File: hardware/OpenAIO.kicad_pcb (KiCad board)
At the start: 6 copper layers, 0 parts

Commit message: Net classes: patterns checked against the per-sheet netlists
VBAT, Phase, Power, Gate (driver outputs only), USB, RF, Analog; priorities
0..6, Default last. Wire widths 12 mil on VBAT and Phase, 8 on Power. Every
pattern verified to match at least one existing net; HIN/LIN, buses and
control signals stay Default.
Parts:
- added AE1: 47948-0001, OpenRX-Shared:ANT-SMD_47948-0001, F.Cu at (138.4, 108.8)
- added AE2: 2450AT18A100E, OpenRX-Shared:ANT-SMD_L3.2-W1.6, F.Cu at (133.5, 108.1)
- added C1: 100n, Capacitor_SMD:C_0201_0603Metric, F.Cu at (122.2, 72.0)
- added C10: 20p, Capacitor_SMD:C_0201_0603Metric, F.Cu at (124.7, 72.0)
- added C11: 100n, Capacitor_SMD:C_0201_0603Metric, F.Cu at (124.7, 73.7)
- added C12: 100n, Capacitor_SMD:C_0201_0603Metric, F.Cu at (124.7, 75.5)
- added C13: 100n, Capacitor_SMD:C_0201_0603Metric, F.Cu at (124.7, 77.2)
- added C14: 100n, Capacitor_SMD:C_0201_0603Metric, F.Cu at (124.7, 79.0)
- added C15: 4.7uF, Capacitor_SMD:C_0402_1005Metric, F.Cu at (141.7, 83.1)
- added C16: 4.7uF, Capacitor_SMD:C_0402_1005Metric, F.Cu at (141.7, 85.0)
- added C17: 4.7uF, Capacitor_SMD:C_0402_1005Metric, F.Cu at (141.7, 87.0)
- added C18: 4.7uF 50v, Capacitor_SMD:C_0805_2012Metric, F.Cu at (81.8, 13.2)
- added C19: 4.7uF 50v, Capacitor_SMD:C_0805_2012Metric, F.Cu at (81.8, 16.2)
- added C2: 100n, Capacitor_SMD:C_0201_0603Metric, F.Cu at (122.2, 73.7)
- added C20: 100n, Capacitor_SMD:C_0201_0603Metric, F.Cu at (64.7, 12.5)
- added C21: 100n, Capacitor_SMD:C_0201_0603Metric, F.Cu at (64.7, 14.3)
- added C22: 100nF, Capacitor_SMD:C_0201_0603Metric, F.Cu at (64.7, 16.0)
- added C23: 22uF, Capacitor_SMD:C_0603_1608Metric, F.Cu at (82.3, 24.6)
- added C24: 22uF, Capacitor_SMD:C_0603_1608Metric, F.Cu at (82.3, 27.1)
- added C25: 4.7uF, Capacitor_SMD:C_0402_1005Metric, F.Cu at (65.0, 28.4)
- added C26: 100n, Capacitor_SMD:C_0201_0603Metric, F.Cu at (64.7, 17.8)
- added C27: 22uF, Capacitor_SMD:C_0402_1005Metric, F.Cu at (65.0, 30.3)
- added C28: 22uF, Capacitor_SMD:C_0402_1005Metric, F.Cu at (65.0, 32.3)
- added C29: 100n, Capacitor_SMD:C_0201_0603Metric, F.Cu at (169.5, 72.0)
- added C3: 4.7uF, Capacitor_SMD:C_0402_1005Metric, F.Cu at (141.7, 81.1)
- added C30: 100n, Capacitor_SMD:C_0201_0603Metric, F.Cu at (169.5, 73.7)
- added C31: 470p, Capacitor_SMD:C_0201_0603Metric, F.Cu at (162.0, 95.6)
- added C32: 100n, Capacitor_SMD:C_0201_0603Metric, F.Cu at (162.0, 97.4)
- added C33: 1uF, Capacitor_SMD:C_0402_1005Metric, F.Cu at (169.6, 95.7)
- added C34: 100n, Capacitor_SMD:C_0201_0603Metric, F.Cu at (162.0, 99.1)
- added C35: 100n, Capacitor_SMD:C_0201_0603Metric, F.Cu at (162.0, 100.9)
- added C36: 100n, Capacitor_SMD:C_0201_0603Metric, F.Cu at (146.7, 103.1)
- added C37: 100nF, Capacitor_SMD:C_0201_0603Metric, F.Cu at (139.7, 7.56)
- added C38: 100nF, Capacitor_SMD:C_0201_0603Metric, F.Cu at (139.7, 9.31)
- added C39: 100nF, Capacitor_SMD:C_0201_0603Metric, F.Cu at (139.7, 11.1)
- added C4: 20p, Capacitor_SMD:C_0201_0603Metric, F.Cu at (122.2, 75.5)
- added C40: 100nF, Capacitor_SMD:C_0402_WIDE, F.Cu at (142.9, 18.2)
- added C41: 100nF, Capacitor_SMD:C_0402_WIDE, F.Cu at (142.9, 20.1)
- added C42: 100nF, Capacitor_SMD:C_0402_WIDE, F.Cu at (142.9, 22.1)
- added C43: 100nF, Capacitor_SMD:C_0201_0603Metric, F.Cu at (139.7, 12.8)
- added C44: 100nF, Capacitor_SMD:C_0201_0603Metric, F.Cu at (105.4, 8.14)
- added C45: 100nF, Capacitor_SMD:C_0201_0603Metric, F.Cu at (105.4, 9.89)
- added C46: 100nF, Capacitor_SMD:C_0201_0603Metric, F.Cu at (105.4, 11.6)
- added C47: 100nF, Capacitor_SMD:C_0402_WIDE, F.Cu at (108.6, 18.8)
- added C48: 100nF, Capacitor_SMD:C_0402_WIDE, F.Cu at (108.6, 20.7)
- added C49: 100nF, Capacitor_SMD:C_0402_WIDE, F.Cu at (108.6, 22.7)
- added C5: 100n, Capacitor_SMD:C_0201_0603Metric, F.Cu at (122.2, 77.2)
- added C50: 100nF, Capacitor_SMD:C_0201_0603Metric, F.Cu at (105.4, 13.4)
- added C51: 100nF, Capacitor_SMD:C_0201_0603Metric, F.Cu at (122.3, 8.31)
- added C52: 100nF, Capacitor_SMD:C_0201_0603Metric, F.Cu at (122.3, 10.1)
- added C53: 100nF, Capacitor_SMD:C_0201_0603Metric, F.Cu at (122.3, 11.8)
- added C54: 100nF, Capacitor_SMD:C_0402_WIDE, F.Cu at (125.6, 18.9)
- added C55: 100nF, Capacitor_SMD:C_0402_WIDE, F.Cu at (125.6, 20.9)
- added C56: 100nF, Capacitor_SMD:C_0402_WIDE, F.Cu at (125.6, 22.9)
- added C57: 100nF, Capacitor_SMD:C_0201_0603Metric, F.Cu at (122.3, 13.6)
- added C58: 100nF, Capacitor_SMD:C_0201_0603Metric, F.Cu at (157.1, 7.17)
- added C59: 100nF, Capacitor_SMD:C_0201_0603Metric, F.Cu at (157.1, 8.92)
- added C6: 100n, Capacitor_SMD:C_0201_0603Metric, F.Cu at (122.2, 79.0)
- added C60: 100nF, Capacitor_SMD:C_0201_0603Metric, F.Cu at (157.1, 10.7)
- added C61: 100nF, Capacitor_SMD:C_0402_WIDE, F.Cu at (160.4, 17.8)
- added C62: 100nF, Capacitor_SMD:C_0402_WIDE, F.Cu at (160.4, 19.8)
- added C63: 100nF, Capacitor_SMD:C_0402_WIDE, F.Cu at (160.4, 21.7)
- added C64: 100nF, Capacitor_SMD:C_0201_0603Metric, F.Cu at (157.1, 12.4)
- added C65: 100nF, Capacitor_SMD:C_0201_0603Metric, F.Cu at (122.2, 94.4)
- added C66: 100nF, Capacitor_SMD:C_0201_0603Metric, F.Cu at (122.2, 96.2)
- added C67: 10nF, Capacitor_SMD:C_0201_0603Metric, F.Cu at (122.2, 97.9)
- added C68: 470nF, Capacitor_SMD:C_0201_0603Metric, F.Cu at (122.2, 99.7)
- added C69: 1nF, Capacitor_SMD:C_0201_0603Metric, F.Cu at (122.2, 101.4)
- added C7: 100n, Capacitor_SMD:C_0201_0603Metric, F.Cu at (122.2, 80.7)
- added C70: 100nF, Capacitor_SMD:C_0201_0603Metric, F.Cu at (122.2, 103.2)
- added C71: 100nF, Capacitor_SMD:C_0201_0603Metric, F.Cu at (122.2, 104.9)
- added C72: 15pF, Capacitor_SMD:C_0201_0603Metric, F.Cu at (122.2, 106.7)
- added C73: 10nF, Capacitor_SMD:C_0201_0603Metric, F.Cu at (124.7, 94.4)
- added C74: 15pF, Capacitor_SMD:C_0201_0603Metric, F.Cu at (124.7, 96.2)
- added C75: 10uF, Capacitor_SMD:C_0402_1005Metric, F.Cu at (139.9, 94.5)
- added C76: 100nF, Capacitor_SMD:C_0201_0603Metric, F.Cu at (124.7, 97.9)
- added C77: 1uF, Capacitor_SMD:C_0201_0603Metric, F.Cu at (124.7, 99.7)
- added C78: 100nF, Capacitor_SMD:C_0201_0603Metric, F.Cu at (124.7, 101.4)
- added C79: 100nF, Capacitor_SMD:C_0201_0603Metric, F.Cu at (124.7, 103.2)
- added C8: 100n, Capacitor_SMD:C_0201_0603Metric, F.Cu at (122.2, 82.5)
- added C80: 10nF, Capacitor_SMD:C_0201_0603Metric, F.Cu at (124.7, 104.9)
- added C81: 1uF, Capacitor_SMD:C_0201_0603Metric, F.Cu at (124.7, 106.7)
- added C82: 10uF, Capacitor_SMD:C_0402_1005Metric, F.Cu at (139.9, 96.5)
- added C83: 1uF, Capacitor_SMD:C_0201_0603Metric, F.Cu at (127.1, 94.4)
- added C84: 1uF, Capacitor_SMD:C_0201_0603Metric, F.Cu at (127.1, 96.2)
- added C85: 1uF, Capacitor_SMD:C_0201_0603Metric, F.Cu at (127.1, 97.9)
- added C86: 1uF, Capacitor_SMD:C_0201_0603Metric, F.Cu at (127.1, 99.7)
- added C87: 1.2pF, Capacitor_SMD:C_0201_0603Metric, F.Cu at (127.1, 101.4)
- added C88: 10uF, Capacitor_SMD:C_0402_1005Metric, F.Cu at (139.9, 98.5)
- added C89: 1.2pF, Capacitor_SMD:C_0201_0603Metric, F.Cu at (127.1, 103.2)
- added C9: 100n, Capacitor_SMD:C_0201_0603Metric, F.Cu at (122.2, 84.2)
- added Card1: TF-021B-H265, lib:TF-SMD_TF-021B-H265, F.Cu at (152.2, 98.4)
- added D1: LED_1_Blue, LED_SMD:LED_0402_1005Metric, F.Cu at (122.7, 89.3)
- added D2: DSK24, lib:SOD-123_L2.8-W1.8-LS3.7-RD, F.Cu at (70.8, 24.7)
- added D3: DSK24, lib:SOD-123_L2.8-W1.8-LS3.7-RD, F.Cu at (70.8, 27.6)
- added D4: LED_1_Green, LED_SMD:LED_0402_1005Metric, F.Cu at (75.1, 24.3)
- added D5: LED_1_Green, LED_SMD:LED_0402_1005Metric, F.Cu at (75.1, 26.3)
- added D6: LED_1_Green, LED_SMD:LED_0402_1005Metric, F.Cu at (75.1, 28.3)
- added D7: LED_1_Green, LED_SMD:LED_0402_1005Metric, F.Cu at (75.1, 30.3)
- added D8: SDM02U30LP3-7B, lib:X3-DFN0603-2_L0.6-W0.3-RD, F.Cu at (169.3, 99.8)
- added D9: XL-1010RGBC-WS2812B, OpenRX-Shared:LED-SMD_4P-L1.0-W1.0-TL_XL-1010RGBC-WS2812B, F.Cu at (128.9, 108.9)
- added FL1: 2450FM07D0034T, OpenRX-Shared:FILTER-SMD_4P-L1.0-W0.5-L, F.Cu at (126.1, 111.3)
- added J1: 5V, lib:small_pad, F.Cu at (105.7, 102.4)
- added J10: 5V, lib:small_pad, F.Cu at (112.3, 104.8)
- added J11: 5V, lib:small_pad, F.Cu at (112.3, 107.2)
- added J12: 5V, lib:small_pad, F.Cu at (112.3, 109.6)
- added J13: 5V, lib:small_pad, F.Cu at (67.1, 47.0)
- added J14: 5V, lib:small_pad, F.Cu at (69.5, 47.0)
- added J2: 5V, lib:small_pad, F.Cu at (105.7, 104.8)
- added J21: 5V, lib:small_pad, F.Cu at (124.7, 46.0)
- added J23: 5V, lib:small_pad, F.Cu at (124.7, 48.4)
- added J25: 5V, lib:small_pad, F.Cu at (124.7, 50.8)
- added J26: 5V, lib:small_pad, F.Cu at (124.7, 53.2)
- added J28: 5V, lib:small_pad, F.Cu at (124.7, 55.6)
- added J29: 5V, lib:small_pad, F.Cu at (124.7, 58.0)
- added J3: 5V, lib:small_pad, F.Cu at (105.7, 107.2)
- added J30: 5V, lib:small_pad, F.Cu at (128.0, 46.0)
- added J32: 5V, lib:small_pad, F.Cu at (128.0, 48.4)
- added J33: 5V, lib:small_pad, F.Cu at (128.0, 50.8)
- added J34: 5V, lib:small_pad, F.Cu at (128.0, 53.2)
- added J35: 5V, lib:small_pad, F.Cu at (128.0, 55.6)
- added J36: 5V, lib:small_pad, F.Cu at (128.0, 58.0)
- added J37: 5V, lib:small_pad, F.Cu at (131.3, 46.0)
- added J38: 5V, lib:small_pad, F.Cu at (131.3, 48.4)
- added J39: 5V, lib:small_pad, F.Cu at (131.3, 50.8)
- added J4: 5V, lib:small_pad, F.Cu at (105.7, 109.6)
- added J42: 5V, lib:small_pad, F.Cu at (131.3, 53.2)
- added J43: 5V, lib:small_pad, F.Cu at (131.3, 55.6)
- added J44: 5V, lib:small_pad, F.Cu at (131.3, 58.0)
- added J45: 5V, lib:small_pad, F.Cu at (134.6, 46.0)
- added J48: 5V, lib:small_pad, F.Cu at (134.6, 48.4)
- added J49: 5V, lib:small_pad, F.Cu at (134.6, 50.8)
- added J5: 5V, lib:small_pad, F.Cu at (109.0, 102.4)
- added J50: 5V, lib:small_pad, F.Cu at (134.6, 53.2)
- added J51: 5V, lib:small_pad, F.Cu at (134.6, 55.6)
- added J6: 5V, lib:small_pad, F.Cu at (109.0, 104.8)
- added J7: 5V, lib:small_pad, F.Cu at (109.0, 107.2)
- added J8: 5V, lib:small_pad, F.Cu at (109.0, 109.6)
- added J9: 5V, lib:small_pad, F.Cu at (112.3, 102.4)
- added L1: AOTA-B201610S3R3-101-T, lib:IND-SMD_L2.0-W1.6_AOTA-B201610S3R3-101-T, F.Cu at (127.7, 86.9)
- added L2: XRTC303020D4R7MBCA, lib:IND-SMD_L3.0-W3.0_AFE303020S, F.Cu at (70.2, 21.0)
- added L3: XRTC303020D4R7MBCA, lib:IND-SMD_L3.0-W3.0_AFE303020S, F.Cu at (74.5, 21.0)
- added L4: 15uH, Inductor_SMD:L_0805_2012Metric, F.Cu at (133.1, 111.0)
- added L5: 24nH, Inductor_SMD:L_0201_0603Metric, F.Cu at (127.1, 104.9)
- added L6: 2.0nH, Inductor_SMD:L_0201_0603Metric, F.Cu at (127.1, 106.7)
- added L7: 2.5nH, Inductor_SMD:L_0201_0603Metric, F.Cu at (129.6, 94.4)
- added OSC1: OW7EL89CENUNFAYLC-52M, OpenRX-Shared:OSC-SMD_4P-L2.0-W1.6-BL_TXC_7Z, F.Cu at (138.8, 102.3)
- added Q1: AP1606, lib:DFN-3L_L1.0-W0.6-P0.65-BR, F.Cu at (141.4, 88.9)
- added Q10: DOY180N03T, Package_SON:Diodes_PowerDI3333-8, F.Cu at (101.8, 14.4)
- added Q11: DOY180N03T, Package_SON:Diodes_PowerDI3333-8, F.Cu at (101.8, 19.1)
- added Q12: DOY180N03T, Package_SON:Diodes_PowerDI3333-8, F.Cu at (101.8, 23.8)
- added Q13: DOY180N03T, Package_SON:Diodes_PowerDI3333-8, F.Cu at (101.8, 28.5)
- added Q14: DOY180N03T, Package_SON:Diodes_PowerDI3333-8, F.Cu at (101.8, 33.2)
- added Q15: DOY180N03T, Package_SON:Diodes_PowerDI3333-8, F.Cu at (118.7, 9.93)
- added Q16: DOY180N03T, Package_SON:Diodes_PowerDI3333-8, F.Cu at (118.7, 14.6)
- added Q17: DOY180N03T, Package_SON:Diodes_PowerDI3333-8, F.Cu at (118.7, 19.3)
- added Q18: DOY180N03T, Package_SON:Diodes_PowerDI3333-8, F.Cu at (118.7, 24.0)
- added Q19: DOY180N03T, Package_SON:Diodes_PowerDI3333-8, F.Cu at (118.7, 28.7)
- added Q2: AP1606, lib:DFN-3L_L1.0-W0.6-P0.65-BR, F.Cu at (141.4, 90.7)
- added Q20: DOY180N03T, Package_SON:Diodes_PowerDI3333-8, F.Cu at (118.7, 33.4)
- added Q21: DOY180N03T, Package_SON:Diodes_PowerDI3333-8, F.Cu at (153.5, 8.79)
- added Q22: DOY180N03T, Package_SON:Diodes_PowerDI3333-8, F.Cu at (153.5, 13.5)
- added Q23: DOY180N03T, Package_SON:Diodes_PowerDI3333-8, F.Cu at (153.5, 18.2)
- added Q24: DOY180N03T, Package_SON:Diodes_PowerDI3333-8, F.Cu at (153.5, 22.9)
- added Q25: DOY180N03T, Package_SON:Diodes_PowerDI3333-8, F.Cu at (153.5, 27.5)
- added Q26: DOY180N03T, Package_SON:Diodes_PowerDI3333-8, F.Cu at (153.5, 32.2)
- added Q3: DOY180N03T, Package_SON:Diodes_PowerDI3333-8, F.Cu at (136.1, 9.18)
- added Q4: DOY180N03T, Package_SON:Diodes_PowerDI3333-8, F.Cu at (136.1, 13.9)
- added Q5: DOY180N03T, Package_SON:Diodes_PowerDI3333-8, F.Cu at (136.1, 18.6)
- added Q6: DOY180N03T, Package_SON:Diodes_PowerDI3333-8, F.Cu at (136.1, 23.2)
- added Q7: DOY180N03T, Package_SON:Diodes_PowerDI3333-8, F.Cu at (136.1, 27.9)
- added Q8: DOY180N03T, Package_SON:Diodes_PowerDI3333-8, F.Cu at (136.1, 32.6)
- added Q9: DOY180N03T, Package_SON:Diodes_PowerDI3333-8, F.Cu at (101.8, 9.76)
- added R1: 100k, Resistor_SMD:R_0201_0603Metric, F.Cu at (124.7, 80.7)
- added R10: 30R, Resistor_SMD:R_0201_0603Metric, F.Cu at (127.1, 82.5)
- added R100: 15R, Resistor_SMD:R_0201_0603Metric, F.Cu at (162.0, 7.17)
- added R101: 15R, Resistor_SMD:R_0201_0603Metric, F.Cu at (162.0, 8.92)
- added R102: 10k, Resistor_SMD:R_0201_0603Metric, F.Cu at (162.0, 10.7)
- added R103: 1k, Resistor_SMD:R_0201_0603Metric, F.Cu at (162.0, 12.4)
- added R104: 10k, Resistor_SMD:R_0201_0603Metric, F.Cu at (162.0, 14.2)
- added R105: 10k, Resistor_SMD:R_0201_0603Metric, F.Cu at (162.0, 15.9)
- added R106: 1k, Resistor_SMD:R_0201_0603Metric, F.Cu at (164.5, 7.17)
- added R107: 10k, Resistor_SMD:R_0201_0603Metric, F.Cu at (164.5, 8.92)
- added R108: 10k, Resistor_SMD:R_0201_0603Metric, F.Cu at (164.5, 10.7)
- added R109: 1k, Resistor_SMD:R_0201_0603Metric, F.Cu at (164.5, 12.4)
- added R11: 5.1k, Resistor_SMD:R_0201_0603Metric, F.Cu at (127.1, 84.2)
- added R110: 10k, Resistor_SMD:R_0201_0603Metric, F.Cu at (164.5, 14.2)
- added R111: 10k, Resistor_SMD:R_0201_0603Metric, F.Cu at (129.6, 96.2)
- added R112: 10k, Resistor_SMD:R_0201_0603Metric, F.Cu at (129.6, 97.9)
- added R113: 10k, Resistor_SMD:R_0201_0603Metric, F.Cu at (129.6, 99.7)
- added R114: 10k, Resistor_SMD:R_0201_0603Metric, F.Cu at (129.6, 101.4)
- added R12: 5.1k, Resistor_SMD:R_0201_0603Metric, F.Cu at (129.6, 72.0)
- added R13: 100k, Resistor_SMD:R_0201_0603Metric, F.Cu at (129.6, 73.7)
- added R14: 2.4k, Resistor_SMD:R_0201_0603Metric, F.Cu at (129.6, 75.5)
- added R15: 75R, Resistor_SMD:R_0201_0603Metric, F.Cu at (129.6, 77.2)
- added R16: 75R, Resistor_SMD:R_0201_0603Metric, F.Cu at (129.6, 79.0)
- added R17: 100k, Resistor_SMD:R_0201_0603Metric, F.Cu at (67.2, 12.5)
- added R18: 6.49k, Resistor_SMD:R_0201_0603Metric, F.Cu at (67.2, 14.3)
- added R19: 100k, Resistor_SMD:R_0201_0603Metric, F.Cu at (67.2, 16.0)
- added R2: 10k, Resistor_SMD:R_0201_0603Metric, F.Cu at (124.7, 82.5)
- added R20: 13.7k, Resistor_SMD:R_0201_0603Metric, F.Cu at (67.2, 17.8)
- added R21: 7.5k, Resistor_SMD:R_0201_0603Metric, F.Cu at (69.6, 12.5)
- added R22: 2.4k, Resistor_SMD:R_0201_0603Metric, F.Cu at (69.6, 14.3)
- added R23: 6.49k, Resistor_SMD:R_0201_0603Metric, F.Cu at (69.6, 16.0)
- added R24: 510R, Resistor_SMD:R_0201_0603Metric, F.Cu at (69.6, 17.8)
- added R25: 10k, Resistor_SMD:R_0201_0603Metric, F.Cu at (169.5, 75.5)
- added R26: 75R, Resistor_SMD:R_0201_0603Metric, F.Cu at (164.5, 95.6)
- added R27: 3.9k, Resistor_SMD:R_0201_0603Metric, F.Cu at (164.5, 97.4)
- added R28: 12k, Resistor_SMD:R_0201_0603Metric, F.Cu at (164.5, 99.1)
- added R29: 1.4k, Resistor_SMD:R_0201_0603Metric, F.Cu at (164.5, 100.9)
- added R3: 5.1k, Resistor_SMD:R_0201_0603Metric, F.Cu at (124.7, 84.2)
- added R30: 680R, Resistor_SMD:R_0201_0603Metric, F.Cu at (166.9, 95.6)
- added R31: 510R, Resistor_SMD:R_0201_0603Metric, F.Cu at (166.9, 97.4)
- added R32: 510R, Resistor_SMD:R_0201_0603Metric, F.Cu at (166.9, 99.1)
- added R33: 75R, Resistor_SMD:R_0201_0603Metric, F.Cu at (166.9, 100.9)
- added R34: 10k, Resistor_SMD:R_0201_0603Metric, F.Cu at (146.7, 104.8)
- added R35: 15R, Resistor_SMD:R_0201_0603Metric, F.Cu at (139.7, 14.6)
- added R36: 15R, Resistor_SMD:R_0201_0603Metric, F.Cu at (139.7, 16.3)
- added R37: 10k, Resistor_SMD:R_0201_0603Metric, F.Cu at (142.1, 7.56)
- added R38: 10k, Resistor_SMD:R_0201_0603Metric, F.Cu at (142.1, 9.31)
- added R39: 220R, Resistor_SMD:R_0201_0603Metric, F.Cu at (142.1, 11.1)
- added R4: 5.1k, Resistor_SMD:R_0201_0603Metric, F.Cu at (127.1, 72.0)
- added R40: 10R, Resistor_SMD:R_0201_0603Metric, F.Cu at (142.1, 12.8)
- added R41: 15R, Resistor_SMD:R_0201_0603Metric, F.Cu at (142.1, 14.6)
- added R42: 15R, Resistor_SMD:R_0201_0603Metric, F.Cu at (142.1, 16.3)
- added R43: 15R, Resistor_SMD:R_0201_0603Metric, F.Cu at (144.6, 7.56)
- added R44: 15R, Resistor_SMD:R_0201_0603Metric, F.Cu at (144.6, 9.31)
- added R45: 10k, Resistor_SMD:R_0201_0603Metric, F.Cu at (144.6, 11.1)
- added R46: 1k, Resistor_SMD:R_0201_0603Metric, F.Cu at (144.6, 12.8)
- added R47: 10k, Resistor_SMD:R_0201_0603Metric, F.Cu at (144.6, 14.6)
- added R48: 10k, Resistor_SMD:R_0201_0603Metric, F.Cu at (144.6, 16.3)
- added R49: 1k, Resistor_SMD:R_0201_0603Metric, F.Cu at (147.0, 7.56)
- added R5: 1k, Resistor_SMD:R_0201_0603Metric, F.Cu at (127.1, 73.7)
- added R50: 10k, Resistor_SMD:R_0201_0603Metric, F.Cu at (147.0, 9.31)
- added R51: 10k, Resistor_SMD:R_0201_0603Metric, F.Cu at (147.0, 11.1)
- added R52: 1k, Resistor_SMD:R_0201_0603Metric, F.Cu at (147.0, 12.8)
- added R53: 10k, Resistor_SMD:R_0201_0603Metric, F.Cu at (147.0, 14.6)
- added R54: 15R, Resistor_SMD:R_0201_0603Metric, F.Cu at (105.4, 15.1)
- added R55: 15R, Resistor_SMD:R_0201_0603Metric, F.Cu at (105.4, 16.9)
- added R56: 10k, Resistor_SMD:R_0201_0603Metric, F.Cu at (107.8, 8.14)
- added R57: 10k, Resistor_SMD:R_0201_0603Metric, F.Cu at (107.8, 9.89)
- added R58: 220R, Resistor_SMD:R_0201_0603Metric, F.Cu at (107.8, 11.6)
- added R59: 10R, Resistor_SMD:R_0201_0603Metric, F.Cu at (107.8, 13.4)
- added R6: 1k, Resistor_SMD:R_0201_0603Metric, F.Cu at (127.1, 75.5)
- added R60: 15R, Resistor_SMD:R_0201_0603Metric, F.Cu at (107.8, 15.1)
- added R61: 15R, Resistor_SMD:R_0201_0603Metric, F.Cu at (107.8, 16.9)
- added R62: 15R, Resistor_SMD:R_0201_0603Metric, F.Cu at (110.3, 8.14)
- added R63: 15R, Resistor_SMD:R_0201_0603Metric, F.Cu at (110.3, 9.89)
- added R64: 10k, Resistor_SMD:R_0201_0603Metric, F.Cu at (110.3, 11.6)
- added R65: 1k, Resistor_SMD:R_0201_0603Metric, F.Cu at (110.3, 13.4)
- added R66: 10k, Resistor_SMD:R_0201_0603Metric, F.Cu at (110.3, 15.1)
- added R67: 10k, Resistor_SMD:R_0201_0603Metric, F.Cu at (110.3, 16.9)
- added R68: 1k, Resistor_SMD:R_0201_0603Metric, F.Cu at (112.7, 8.14)
- added R69: 10k, Resistor_SMD:R_0201_0603Metric, F.Cu at (112.7, 9.89)
- added R7: 10k, Resistor_SMD:R_0201_0603Metric, F.Cu at (127.1, 77.2)
- added R70: 10k, Resistor_SMD:R_0201_0603Metric, F.Cu at (112.7, 11.6)
- added R71: 1k, Resistor_SMD:R_0201_0603Metric, F.Cu at (112.7, 13.4)
- added R72: 10k, Resistor_SMD:R_0201_0603Metric, F.Cu at (112.7, 15.1)
- added R73: 15R, Resistor_SMD:R_0201_0603Metric, F.Cu at (122.3, 15.3)
- added R74: 15R, Resistor_SMD:R_0201_0603Metric, F.Cu at (122.3, 17.1)
- added R75: 10k, Resistor_SMD:R_0201_0603Metric, F.Cu at (124.7, 8.31)
- added R76: 10k, Resistor_SMD:R_0201_0603Metric, F.Cu at (124.7, 10.1)
- added R77: 220R, Resistor_SMD:R_0201_0603Metric, F.Cu at (124.7, 11.8)
- added R78: 10R, Resistor_SMD:R_0201_0603Metric, F.Cu at (124.7, 13.6)
- added R79: 15R, Resistor_SMD:R_0201_0603Metric, F.Cu at (124.7, 15.3)
- added R8: 30R, Resistor_SMD:R_0201_0603Metric, F.Cu at (127.1, 79.0)
- added R80: 15R, Resistor_SMD:R_0201_0603Metric, F.Cu at (124.7, 17.1)
- added R81: 15R, Resistor_SMD:R_0201_0603Metric, F.Cu at (127.2, 8.31)
- added R82: 15R, Resistor_SMD:R_0201_0603Metric, F.Cu at (127.2, 10.1)
- added R83: 10k, Resistor_SMD:R_0201_0603Metric, F.Cu at (127.2, 11.8)
- added R84: 1k, Resistor_SMD:R_0201_0603Metric, F.Cu at (127.2, 13.6)
- added R85: 10k, Resistor_SMD:R_0201_0603Metric, F.Cu at (127.2, 15.3)
- added R86: 10k, Resistor_SMD:R_0201_0603Metric, F.Cu at (127.2, 17.1)
- added R87: 1k, Resistor_SMD:R_0201_0603Metric, F.Cu at (129.6, 8.31)
- added R88: 10k, Resistor_SMD:R_0201_0603Metric, F.Cu at (129.6, 10.1)
- added R89: 10k, Resistor_SMD:R_0201_0603Metric, F.Cu at (129.6, 11.8)
- added R9: 30R, Resistor_SMD:R_0201_0603Metric, F.Cu at (127.1, 80.7)
- added R90: 1k, Resistor_SMD:R_0201_0603Metric, F.Cu at (129.6, 13.6)
- added R91: 10k, Resistor_SMD:R_0201_0603Metric, F.Cu at (129.6, 15.3)
- added R92: 15R, Resistor_SMD:R_0201_0603Metric, F.Cu at (157.1, 14.2)
- added R93: 15R, Resistor_SMD:R_0201_0603Metric, F.Cu at (157.1, 15.9)
- added R94: 10k, Resistor_SMD:R_0201_0603Metric, F.Cu at (159.6, 7.17)
- added R95: 10k, Resistor_SMD:R_0201_0603Metric, F.Cu at (159.6, 8.92)
- added R96: 220R, Resistor_SMD:R_0201_0603Metric, F.Cu at (159.6, 10.7)
- added R97: 10R, Resistor_SMD:R_0201_0603Metric, F.Cu at (159.6, 12.4)
- added R98: 15R, Resistor_SMD:R_0201_0603Metric, F.Cu at (159.6, 14.2)
- added R99: 15R, Resistor_SMD:R_0201_0603Metric, F.Cu at (159.6, 15.9)
- added Rsense1: 0.2mR, Resistor_SMD:R_2512_6332Metric, F.Cu at (69.5, 52.9)
- added TP1: TestPoint, TestPoint:TestPoint_Pad_D1.0mm, F.Cu at (140.0, 18.7)
- added TP2: TestPoint, TestPoint:TestPoint_Pad_D1.0mm, F.Cu at (140.0, 21.8)
- added TP3: TestPoint, TestPoint:TestPoint_Pad_D1.0mm, F.Cu at (105.7, 19.3)
- added TP4: TestPoint, TestPoint:TestPoint_Pad_D1.0mm, F.Cu at (105.7, 22.3)
- added TP5: TestPoint, TestPoint:TestPoint_Pad_D1.0mm, F.Cu at (122.6, 19.5)
- added TP6: TestPoint, TestPoint:TestPoint_Pad_D1.0mm, F.Cu at (122.6, 22.5)
- added TP7: TestPoint, TestPoint:TestPoint_Pad_D1.0mm, F.Cu at (157.4, 18.3)
- added TP8: TestPoint, TestPoint:TestPoint_Pad_D1.0mm, F.Cu at (157.4, 21.4)
- added TP9: BOOT, OpenRX-Shared:SolderPad_1.2x2.0mm, F.Cu at (122.6, 109.4)
- added U1: TS2306A 240GF MSM 9_C2976675, lib:SW-SMD_4P-L3.0-W2.0-P0.85-LS3.5, F.Cu at (123.4, 86.7)
- added U10: COS8051SOT, lib:SOT-23-5_L3.0-W1.7-P0.95-LS2.8-BR, F.Cu at (168.3, 103.8)
- added U11: TLV7031DPWR, lib:X2SON-4_L0.8-W0.8-P0.48-TL-A, F.Cu at (169.5, 97.8)
- added U12: SM06B-SRSS-TB(LF)(SN), lib:CONN-SMD_SM06B-SRSS-TB-LF-SN, F.Cu at (81.0, 74.6)
- added U13: AT32F421G8U7, 4in1ESC:QFN-28_L4.0-W4.0-P0.40-TL-EP2.4, F.Cu at (141.1, 31.3)
- added U14: NSG2065Q, 4in1ESC:QFN-24_L4.0-W4.0-P0.50-TL-EP2.8, F.Cu at (141.5, 26.0)
- added U15: AT32F421G8U7, 4in1ESC:QFN-28_L4.0-W4.0-P0.40-TL-EP2.4, F.Cu at (106.8, 31.9)
- added U16: NSG2065Q, 4in1ESC:QFN-24_L4.0-W4.0-P0.50-TL-EP2.8, F.Cu at (107.2, 26.6)
- added U17: AT32F421G8U7, 4in1ESC:QFN-28_L4.0-W4.0-P0.40-TL-EP2.4, F.Cu at (123.7, 32.1)
- added U18: NSG2065Q, 4in1ESC:QFN-24_L4.0-W4.0-P0.50-TL-EP2.8, F.Cu at (124.2, 26.8)
- added U19: AT32F421G8U7, 4in1ESC:QFN-28_L4.0-W4.0-P0.40-TL-EP2.4, F.Cu at (158.5, 30.9)
- added U2: RP2354A, lib:QFN-60_L7.0-W7.0-P0.40-TL-EP3.4, F.Cu at (135.8, 84.6)
- added U20: NSG2065Q, 4in1ESC:QFN-24_L4.0-W4.0-P0.50-TL-EP2.8, F.Cu at (159.0, 25.6)
- added U21: SX1281IMLTRT, OpenRX-Shared:QFN-24_L4.0-W4.0-P0.50-TL-EP2.6, F.Cu at (133.7, 103.7)
- added U22: ESP32-C3, Package_DFN_QFN:QFN-32-1EP_5x5mm_P0.5mm_EP3.7x3.7mm, F.Cu at (134.8, 97.2)
- added U23: TLV75533PDQNR, OpenRX-Shared:X2SON-4_L1.0-W1.0-P0.65-TL-EP, F.Cu at (128.8, 111.4)
- added U3: LMR51430YFDDCR, lib:SOT-23-6_L2.9-W1.6-P0.95-LS2.9-BL, F.Cu at (66.0, 20.8)
- added U4: LMR51430YFDDCR, lib:SOT-23-6_L2.9-W1.6-P0.95-LS2.9-BL, F.Cu at (66.0, 25.2)
- added U5: INA186A3IDCKR, 4in1ESC:SOT-363_SC-70-6, F.Cu at (70.2, 31.1)
- added U6: LP5912-1.8DRVR, lib:WSON-6-1EP_2x2mm_P0.65mm_EP1x1.6mm_ThermalVias, F.Cu at (78.4, 25.2)
- added U7: LP5912-3.3DRVR, Package_SON:WSON-6-1EP_2x2mm_P0.65mm_EP1x1.6mm, F.Cu at (78.4, 28.8)
- added U8: BMI270, lib:LGA-14_L3.0-W2.5-P0.50-BR, F.Cu at (172.9, 73.0)
- added U9: SN74LVC1G3157DTBR, lib:X2SON-6_L1.0-W0.8-BL, F.Cu at (163.4, 104.3)
- added USB1: TYPE-C 16P QTWT, lib:USB-TYPE-C-SMD_TYPE-C-16P-QTWT, F.Cu at (62.9, 55.6)
- added X1: XTM25012000JT00351001, lib:CRYSTAL-SMD_4P-L2.5-W2.0-BL-A, F.Cu at (127.5, 89.9)
- added X2: CJ17-400001010B20, OpenRX-Shared:CRYSTAL-SMD_4P-L1.6-W1.2-BL, F.Cu at (125.9, 108.9)
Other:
- board outline added: 33 x 33 mm

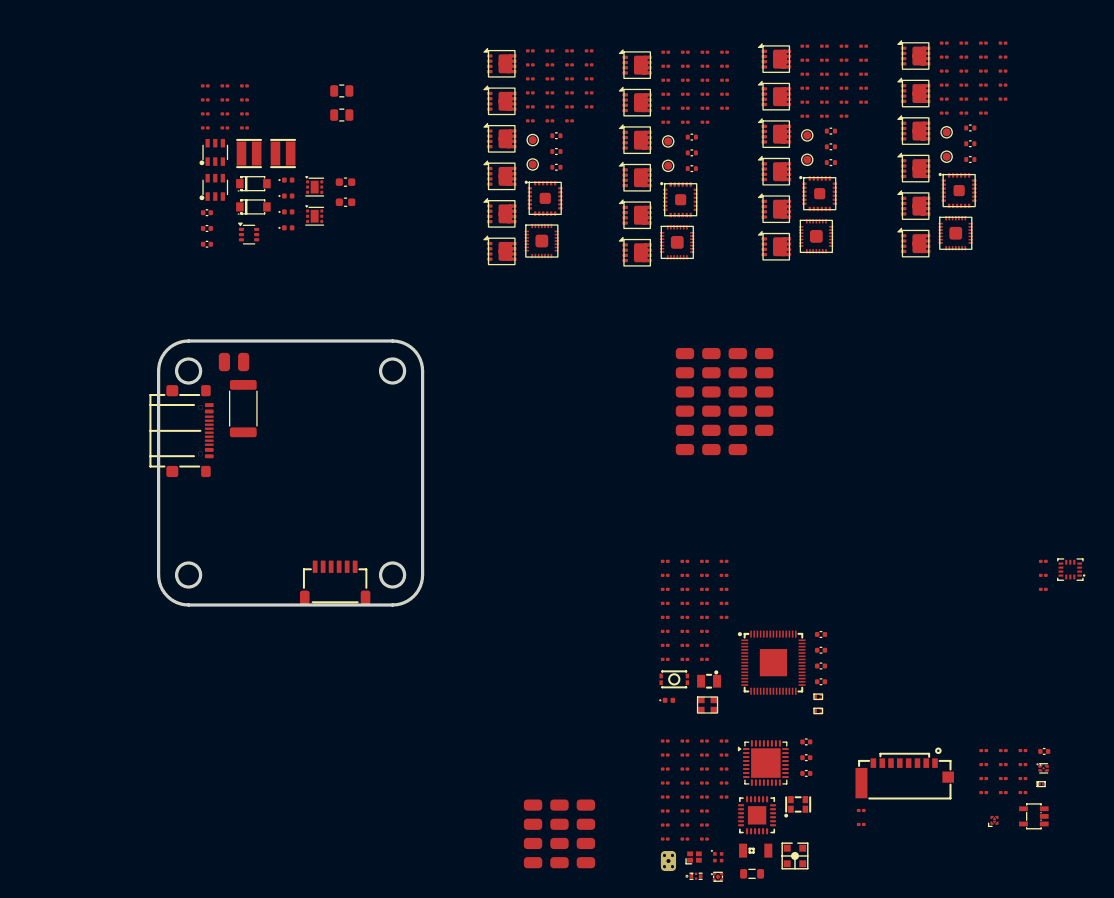
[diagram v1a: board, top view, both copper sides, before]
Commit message: End of day 08-15: schematic mostly wired, first placement and routing
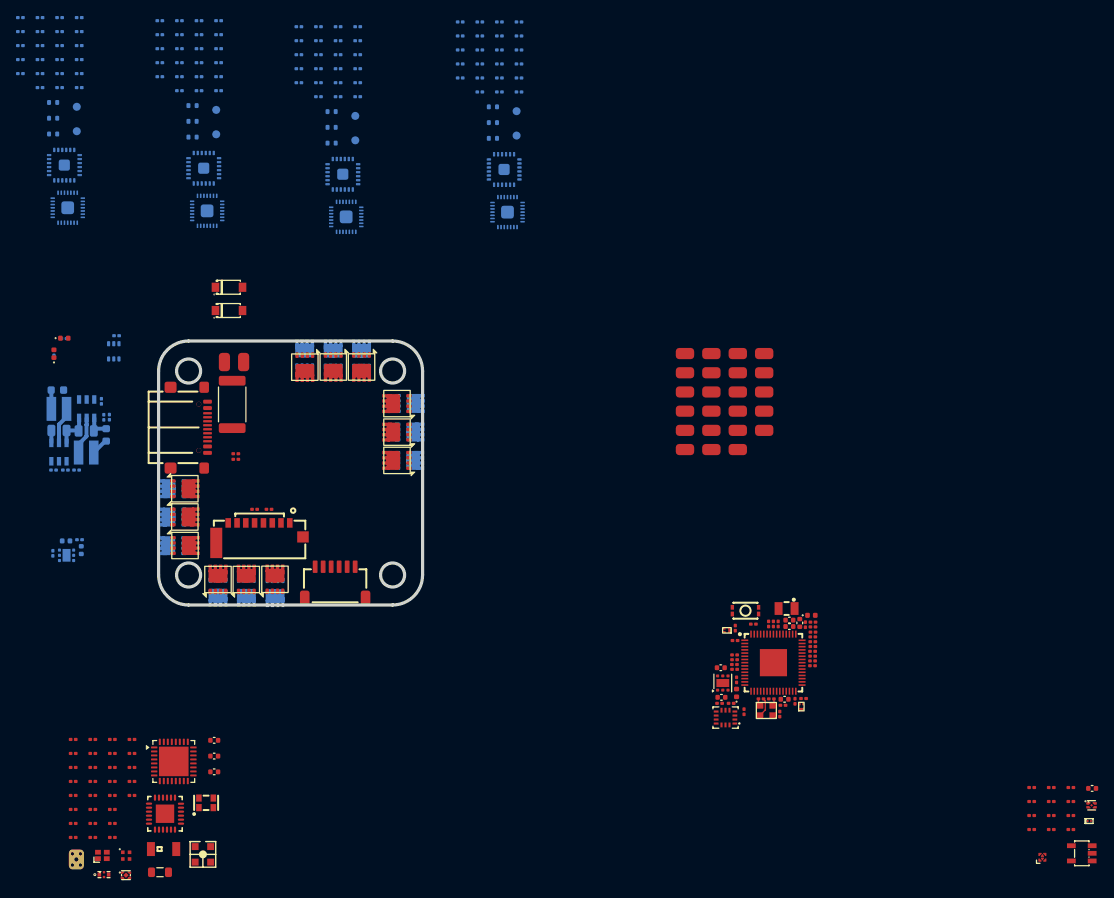
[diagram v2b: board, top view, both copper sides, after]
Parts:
- removed J1, J10, J11, J12, J2, J3, J4, J5, J6, J7, J8, J9: 5V, lib:small_pad
- C18, C19, C20, C21, C22, C23, C24, C26, C28, C37, C38, C39, C40, C41, C42, C43, C44, C45, C46, C47, C48, C49, C50, C51, C52, C53, C54, C55, C56, C57, C58, C59, C60, C61, C62, C63, C64, D6, L2, L3, Q10, Q12, Q14, Q16, Q18, Q20, Q22, Q24, Q26, Q4, Q6, Q8, R100, R101, R102, R103, R104, R105, R106, R107, R108, R109, R110, R17, R18, R19, R20, R21, R22, R24, R35, R36, R37, R38, R39, R40, R41, R42, R43, R44, R45, R46, R47, R48, R49, R50, R51, R52, R53, R54, R55, R56, R57, R58, R59, R60, R61, R62, R63, R64, R65, R66, R67, R68, R69, R70, R71, R72, R73, R74, R75, R76, R77, R78, R79, R80, R81, R82, R83, R84, R85, R86, R87, R88, R89, R90, R91, R92, R93, R94, R95, R96, R97, R98, R99, TP1, TP2, TP3, TP4, TP5, TP6, TP7, TP8, U13, U14, U15, U16, U17, U18, U19, U20, U3, U4, U5, U7: moved to B.Cu
- moved R106 122.9 mm to (41.6, 3.98), turned to 180 degrees
- moved R107 122.9 mm to (41.6, 5.73), turned to 180 degrees
- moved R108 122.9 mm to (41.6, 7.48), turned to 180 degrees
- moved R109 122.9 mm to (41.6, 9.23), turned to 180 degrees
- moved R110 122.9 mm to (41.6, 11.0), turned to 180 degrees
- moved R100 118.0 mm to (44.1, 3.98), turned to 180 degrees
- moved R101 118.0 mm to (44.1, 5.73), turned to 180 degrees
- moved R102 118.0 mm to (44.1, 7.48), turned to 180 degrees
- moved R103 118.0 mm to (44.1, 9.23), turned to 180 degrees
- moved R104 118.0 mm to (44.1, 11.0), turned to 180 degrees
- moved R105 118.0 mm to (44.1, 12.7), turned to 180 degrees
- moved C61 114.7 mm to (45.7, 14.6), turned to 180 degrees
- moved C62 114.7 mm to (45.7, 16.6), turned to 180 degrees
- moved C63 114.7 mm to (45.7, 18.5), turned to 180 degrees
- moved R94 113.1 mm to (46.5, 3.98), turned to 180 degrees
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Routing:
- net GND: track 0.00 -> 5.76 mm
- net Net-(U3-SW): track 0.00 -> 4.74 mm
- net +BATT: track 0.00 -> 4.72 mm
- net Net-(U4-SW): track 0.00 -> 4.64 mm
- net /RP2354A/XIN: track 0.00 -> 2.45 mm
- net +5V: track 0.00 -> 2.36 mm
- net +10V: track 0.00 -> 2.14 mm
- net Net-(C10-Pad2): track 0.00 -> 0.88 mm

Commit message: OpenAIO: master PCB with Base and Core islands routed, AIO_outline footprint+symbol in project lib
Save point before the two-board (LGA) split tooling.
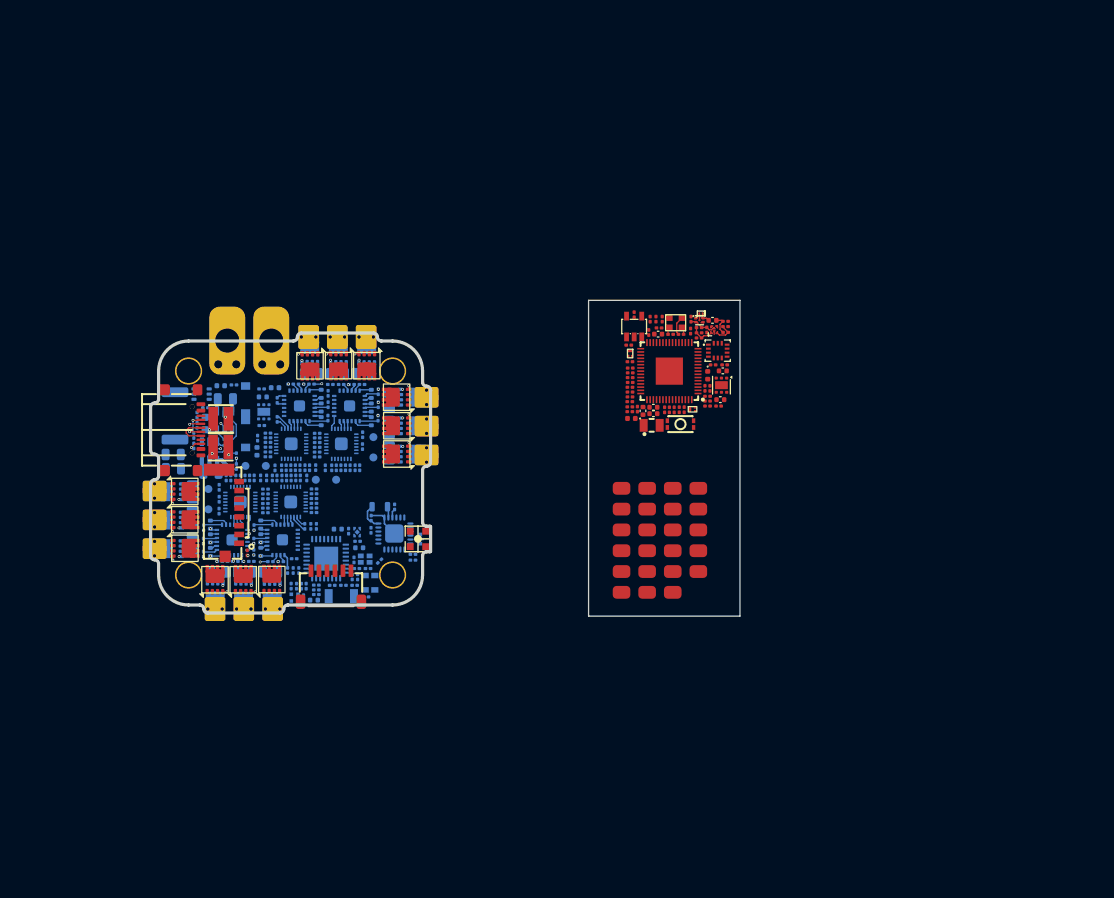
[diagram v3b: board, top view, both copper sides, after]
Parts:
- removed C22: 100nF, Capacitor_SMD:C_0201_0603Metric
- removed J13, J14: 5V, lib:small_pad
- removed Rsense1: 0.2mR, Resistor_SMD:R_2512_6332Metric
- removed TP9: BOOT, OpenRX-Shared:SolderPad_1.2x2.0mm
- removed U5: INA186A3IDCKR, 4in1ESC:SOT-363_SC-70-6
- added C100: C, Capacitor_SMD:C_0805_2012Metric, B.Cu at (87.7, 55.2)
- added C101: C, Capacitor_SMD:C_0805_2012Metric, B.Cu at (87.7, 52.0)
- added C102: C, Capacitor_SMD:C_0805_2012Metric, B.Cu at (60.7, 58.6)
- added C103: C, Capacitor_SMD:C_0805_2012Metric, B.Cu at (60.8, 60.4)
- added C104: 100nF, Capacitor_SMD:C_0201_0603Metric, B.Cu at (64.8, 52.8)
- added C90: C, Capacitor_SMD:C_0805_2012Metric, B.Cu at (63.1, 63.3)
- added C91: C, Capacitor_SMD:C_0805_2012Metric, B.Cu at (63.1, 66.5)
- added C92: C, Capacitor_SMD:C_0805_2012Metric, B.Cu at (63.1, 69.7)
- added C93: C, Capacitor_SMD:C_0805_2012Metric, B.Cu at (66.5, 73.3)
- added C94: C, Capacitor_SMD:C_0805_2012Metric, B.Cu at (69.7, 73.3)
- added C95: C, Capacitor_SMD:C_0805_2012Metric, B.Cu at (72.9, 73.3)
- added C96: C, Capacitor_SMD:C_0805_2012Metric, B.Cu at (84.5, 48.5)
- added C97: C, Capacitor_SMD:C_0805_2012Metric, B.Cu at (81.2, 48.5)
- added C98: C, Capacitor_SMD:C_0805_2012Metric, B.Cu at (78.0, 48.5)
- added C99: C, Capacitor_SMD:C_0805_2012Metric, B.Cu at (87.7, 58.4)
- added Rsense2: 0.2mR, Resistor_SMD:R_2512_6332Metric, B.Cu at (61.0, 53.8)
- added U24: AIO_outline, OpenDrone:AIO_outline, F.Cu at (75.4, 60.9)
- added U25: INA186A3IDCKR, 4in1ESC:SOT-363_SC-70-6, B.Cu at (64.3, 51.0)
- AE2, C36, C65, C66, C67, C68, C69, C70, C71, C72, C73, C74, C75, C76, C77, C78, C79, C80, C81, C82, C83, C84, C85, C86, C87, C88, C89, D2, D3, D4, D5, D9, FL1, L4, L5, L6, L7, OSC1, R111, R112, R113, R114, R3, R4, U21, U22, U23, X2: moved to B.Cu
- L2, L3: moved to F.Cu
- moved U10 86.4 mm to (118.3, 42.6), turned to -90 degrees
- moved R33 82.0 mm to (117.7, 44.9), turned to 180 degrees
- moved R32 81.3 mm to (120.3, 41.7), turned to -90 degrees
- moved C34 79.9 mm to (118.3, 41.1), turned to -90 degrees
- moved D8 79.9 mm to (126.7, 41.0), turned to 180 degrees
- moved R31 79.5 mm to (121.1, 41.7), turned to -90 degrees
- moved U11 78.0 mm to (126.5, 41.8)
- moved U9 77.7 mm to (128.3, 43.0)
- moved C35 76.7 mm to (125.4, 41.7), turned to 90 degrees
- moved R29 76.1 mm to (126.5, 43.4), turned to 180 degrees
- moved C33 75.3 mm to (128.1, 41.8), turned to 180 degrees
- moved R28 75.2 mm to (126.5, 42.7)
- moved R27 72.8 mm to (126.5, 44.0)
- moved R62 72.1 mm to (70.8, 70.8), turned to -90 degrees
- moved C32 71.6 mm to (127.4, 43.0), turned to -90 degrees
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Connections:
- net /ESC1/MotorA renamed /1A
- net /ESC1/MotorB renamed /1B
- net /ESC1/MotorC renamed /1C
- net /ESC2/MotorA renamed /2A
- net /ESC2/MotorB renamed /2B
- net /ESC2/MotorC renamed /2C
- net /ESC3/MotorA renamed /3A
- net /ESC3/MotorB renamed /3B
- net /ESC3/MotorC renamed /3C
- net /ESC4/MotorA renamed /4A
- net /ESC4/MotorB renamed /4B
- net /ESC4/MotorC renamed /4C
- R5 pad 1: /Power/CURR -> /RP2354A/ESC_CURRENT
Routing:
- net GND: track 5.76 -> 20.3 mm
- net +3V3: track 0.00 -> 5.47 mm
- net /RP2354A/D+: track 0.00 -> 4.29 mm
- net +3.3V: track 0.00 -> 3.57 mm, vias 0 -> 1
- net Net-(U21-DCC_FB): track 0.00 -> 3.34 mm
- net /OSD/OSD_LVL: track 0.00 -> 3.05 mm
- net /RP2354A/D-: track 0.00 -> 2.86 mm, vias 0 -> 2
- net /OSD/VIDEO_IN: track 0.00 -> 2.65 mm
- net Net-(USB1-CC1): track 0.00 -> 2.64 mm, vias 0 -> 1
- net /OSD/VID_FILT: track 0.00 -> 2.57 mm
- net /ESC4/GHA: track 0.00 -> 2.33 mm
- net /ESC3/GHA: track 0.00 -> 2.33 mm
- net /ESC1/GHA: track 0.00 -> 2.33 mm
- net /ESC2/GHA: track 0.00 -> 2.33 mm
- net Net-(U20-VB1): track 0.00 -> 2.31 mm
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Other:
- board size 33 x 33 mm -> 35 x 35 mm

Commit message: OpenAIO: two-board stack tooling, Base + Core over an interior LGA
One project, one schematic, one master PCB; the shippable boards are derived.
tools/lga_gen.py: pin table -> Core_LGA_land, Core_LGA_pads (X pre-mirrored
for B.Cu), symbol Core_LGA, core_interface sheet with global labels.
tools/lga_wire_root.py: sheet on the root, global labels on the RP2354A wires,
USB_D+/- in fc_rp2350a, root CURR hier label made global (closes the CSA link).
tools/lga_place.py: J90 on the Base, J91 flipped on the Core, paths set.
tools/split_boards.py: export/OpenAIO-Base and -Core, DRC, Core STEP as J90
3D model plus outline shadow in the master. USB netclass patterns *D+/*D-.
AGENTS.md: architecture, derived boards, layout rules.
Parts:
- added J90: Core_LGA, lib:Core_LGA_land, F.Cu at (75.4, 60.9)
- added J91: Core_LGA, lib:Core_LGA_pads, B.Cu at (123.2, 47.7)
